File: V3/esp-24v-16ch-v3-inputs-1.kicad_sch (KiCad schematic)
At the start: 100 parts, among them U10 OR-3H4-4, U11 OR-3H4-4, U8 OR-3H4-4, U9 OR-3H4-4

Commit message: working on v3
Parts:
- C23, C24, C25, C26, C27, C28, C29, C30, C31, C32, C33, C34, C35, C36, C37, C38: value 33nF/50V/0805 -> 33nF/50V
- D11, D12, D13, D14, D19, D20, D21, D22, D27, D28, D29, D30, D35, D36, D37, D38: footprint Tales:D_MiniMELF -> Tales:D_SOD-123; Case Mini-MELF -> SOD-123; LCSC Part # C8067 -> C19077407; Mfr Semtech -> hongjiacheng; Mfr PN ZMM9V1-M -> BZT52C9V1; Vendor PN C8067 -> C19077407
- R33, R34, R35, R36, R45, R46, R47, R48, R57, R58, R59, R60, R69, R70, R71, R72: value 5,6k/0,1W/0603 -> 5,6k/0,1W
- R37, R38, R39, R40, R49, R50, R51, R52, R61, R62, R63, R64, R73, R74, R75, R76: value 1k8/0,125W/0805 -> 1k8/0,125W
- R41, R42, R43, R44, R53, R54, R55, R56, R65, R66, R67, R68, R77, R78, R79, R80: value 2k2/62,5mW/0402 -> 2k2/62,5mW

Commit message: Final touches to fabrication
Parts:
- D10, D15, D16, D17, D18, D23, D24, D25, D26, D31, D32, D33, D34, D7, D8, D9: Case 0603 -> 0603/1608
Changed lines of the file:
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@@
 			)
 		)
-		(property "Case" "0603"
+		(property "Case" "0603/1608"
 			(at 33.02 46.99 0)
 			(effects
@@
 			)
 		)
-		(property "Case" "0603"
+		(property "Case" "0603/1608"
 			(at 162.56 120.65 0)
 			(effects
@@
 			)
 		)
-		(property "Case" "0603"
+		(property "Case" "0603/1608"
 			(at 97.79 83.82 0)
 			(effects
@@
 			)
 		)
-		(property "Case" "0603"
+		(property "Case" "0603/1608"
 			(at 33.02 83.82 0)
 			(effects
@@
 			)
 		)
-		(property "Case" "0603"
+		(property "Case" "0603/1608"
 			(at 97.79 46.99 0)
 			(effects
@@
 			)
 		)
-		(property "Case" "0603"
+		(property "Case" "0603/1608"
 			(at 227.33 120.65 0)
 			(effects
@@
 			)
 		)
-		(property "Case" "0603"
+		(property "Case" "0603/1608"
 			(at 227.33 46.99 0)
 			(effects
@@
 			)
 		)
-		(property "Case" "0603"
+		(property "Case" "0603/1608"
 			(at 97.79 120.65 0)
 			(effects
@@
 			)
 		)
-		(property "Case" "0603"
+		(property "Case" "0603/1608"
 			(at 33.02 157.48 0)
 			(effects
@@
 			)
 		)
-		(property "Case" "0603"
+		(property "Case" "0603/1608"
 			(at 227.33 83.82 0)
 			(effects
@@
 			)
 		)
-		(property "Case" "0603"
+		(property "Case" "0603/1608"
 			(at 162.56 83.82 0)
 			(effects
@@
 			)
 		)
-		(property "Case" "0603"
+		(property "Case" "0603/1608"
 			(at 33.02 120.65 0)
 			(effects
@@
 			)
 		)
-		(property "Case" "0603"
+		(property "Case" "0603/1608"
 			(at 162.56 46.99 0)
 			(effects
@@
 			)
 		)
-		(property "Case" "0603"
+		(property "Case" "0603/1608"
 			(at 227.33 157.48 0)
 			(effects
@@
 			)
 		)
-		(property "Case" "0603"
+		(property "Case" "0603/1608"
 			(at 97.79 157.48 0)
 			(effects
@@
 			)
 		)
-		(property "Case" "0603"
+		(property "Case" "0603/1608"
 			(at 162.56 157.48 0)
 			(effects

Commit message: Added temperature sensor
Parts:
- R33, R34, R35, R36, R45, R46, R47, R48, R57, R58, R59, R60, R69, R70, R71, R72: value 5,6k/0,1W -> 5,6k/100mW
- R37, R38, R39, R40, R49, R50, R51, R52, R61, R62, R63, R64, R73, R74, R75, R76: value 1k8/0,125W -> 1k8/125mW
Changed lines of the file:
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@@
 			)
 		)
-		(property "Value" "5,6k/0,1W"
+		(property "Value" "5,6k/100mW"
 			(at 224.79 76.2 0)
 			(effects
@@
 			)
 		)
-		(property "Value" "1k8/0,125W"
+		(property "Value" "1k8/125mW"
 			(at 171.45 27.94 90)
 			(effects
@@
 			)
 		)
-		(property "Value" "5,6k/0,1W"
+		(property "Value" "5,6k/100mW"
 			(at 95.25 113.03 0)
 			(effects
@@
 			)
 		)
-		(property "Value" "1k8/0,125W"
+		(property "Value" "1k8/125mW"
 			(at 236.22 138.43 90)
 			(effects
@@
 			)
 		)
-		(property "Value" "1k8/0,125W"
+		(property "Value" "1k8/125mW"
 			(at 106.68 101.6 90)
 			(effects
@@
 			)
 		)
-		(property "Value" "1k8/0,125W"
+		(property "Value" "1k8/125mW"
 			(at 106.68 27.94 90)
 			(effects
@@
 			)
 		)
-		(property "Value" "5,6k/0,1W"
+		(property "Value" "5,6k/100mW"
 			(at 224.79 113.03 0)
 			(effects
@@
 			)
 		)
-		(property "Value" "5,6k/0,1W"
+		(property "Value" "5,6k/100mW"
 			(at 30.48 39.37 0)
 			(effects
@@
 			)
 		)
-		(property "Value" "1k8/0,125W"
+		(property "Value" "1k8/125mW"
 			(at 41.91 101.6 90)
 			(effects
@@
 			)
 		)
-		(property "Value" "5,6k/0,1W"
+		(property "Value" "5,6k/100mW"
 			(at 224.79 39.37 0)
 			(effects
@@
 			)
 		)
-		(property "Value" "5,6k/0,1W"
+		(property "Value" "5,6k/100mW"
 			(at 30.48 113.03 0)
 			(effects
@@
 			)
 		)
-		(property "Value" "5,6k/0,1W"
+		(property "Value" "5,6k/100mW"
 			(at 95.25 39.37 0)
 			(effects
@@
 			)
 		)
-		(property "Value" "5,6k/0,1W"
+		(property "Value" "5,6k/100mW"
 			(at 95.25 149.86 0)
 			(effects
@@
 			)
 		)
-		(property "Value" "5,6k/0,1W"
+		(property "Value" "5,6k/100mW"
 			(at 160.02 149.86 0)
 			(effects
@@
 			)
 		)
-		(property "Value" "1k8/0,125W"
+		(property "Value" "1k8/125mW"
 			(at 106.68 64.77 90)
 			(effects
@@
 			)
 		)
-		(property "Value" "1k8/0,125W"
+		(property "Value" "1k8/125mW"
 			(at 171.45 64.77 90)
 			(effects
@@
 			)
 		)
-		(property "Value" "1k8/0,125W"
+		(property "Value" "1k8/125mW"
 			(at 106.68 138.43 90)
 			(effects
@@
 			)
 		)
-		(property "Value" "5,6k/0,1W"
+		(property "Value" "5,6k/100mW"
 			(at 95.25 76.2 0)
 			(effects
@@
 			)
 		)
-		(property "Value" "5,6k/0,1W"
+		(property "Value" "5,6k/100mW"
 			(at 160.02 76.2 0)
 			(effects
@@
 			)
 		)
-		(property "Value" "1k8/0,125W"
+		(property "Value" "1k8/125mW"
 			(at 236.22 64.77 90)
 			(effects
@@
 			)
 		)
-		(property "Value" "1k8/0,125W"
+		(property "Value" "1k8/125mW"
 			(at 171.45 101.6 90)
 			(effects
@@
 			)
 		)
-		(property "Value" "1k8/0,125W"
+		(property "Value" "1k8/125mW"
 			(at 41.91 64.77 90)
 			(effects
@@
 			)
 		)
-		(property "Value" "5,6k/0,1W"
+		(property "Value" "5,6k/100mW"
 			(at 224.79 149.86 0)
 			(effects
@@
 			)
 		)
-		(property "Value" "5,6k/0,1W"
+		(property "Value" "5,6k/100mW"
 			(at 30.48 76.2 0)
 			(effects
@@
 			)
 		)
-		(property "Value" "1k8/0,125W"
+		(property "Value" "1k8/125mW"
 			(at 236.22 27.94 90)
 			(effects
@@
 			)
 		)
-		(property "Value" "5,6k/0,1W"
+		(property "Value" "5,6k/100mW"
 			(at 160.02 39.37 0)
 			(effects
@@
 			)
 		)
-		(property "Value" "5,6k/0,1W"
+		(property "Value" "5,6k/100mW"
 			(at 160.02 113.03 0)
 			(effects
@@
 			)
 		)
-		(property "Value" "1k8/0,125W"
+		(property "Value" "1k8/125mW"
 			(at 236.22 101.6 90)
 			(effects
@@
 			)
 		)
-		(property "Value" "1k8/0,125W"
+		(property "Value" "1k8/125mW"
 			(at 171.45 138.43 90)
 			(effects
@@
 			)
 		)
-		(property "Value" "5,6k/0,1W"
+		(property "Value" "5,6k/100mW"
 			(at 30.48 149.86 0)
 			(effects
@@
 			)
 		)
-		(property "Value" "1k8/0,125W"
+		(property "Value" "1k8/125mW"
 			(at 41.91 138.43 90)
 			(effects
@@
 			)
 		)
-		(property "Value" "1k8/0,125W"
+		(property "Value" "1k8/125mW"
 			(at 41.91 27.94 90)
 			(effects

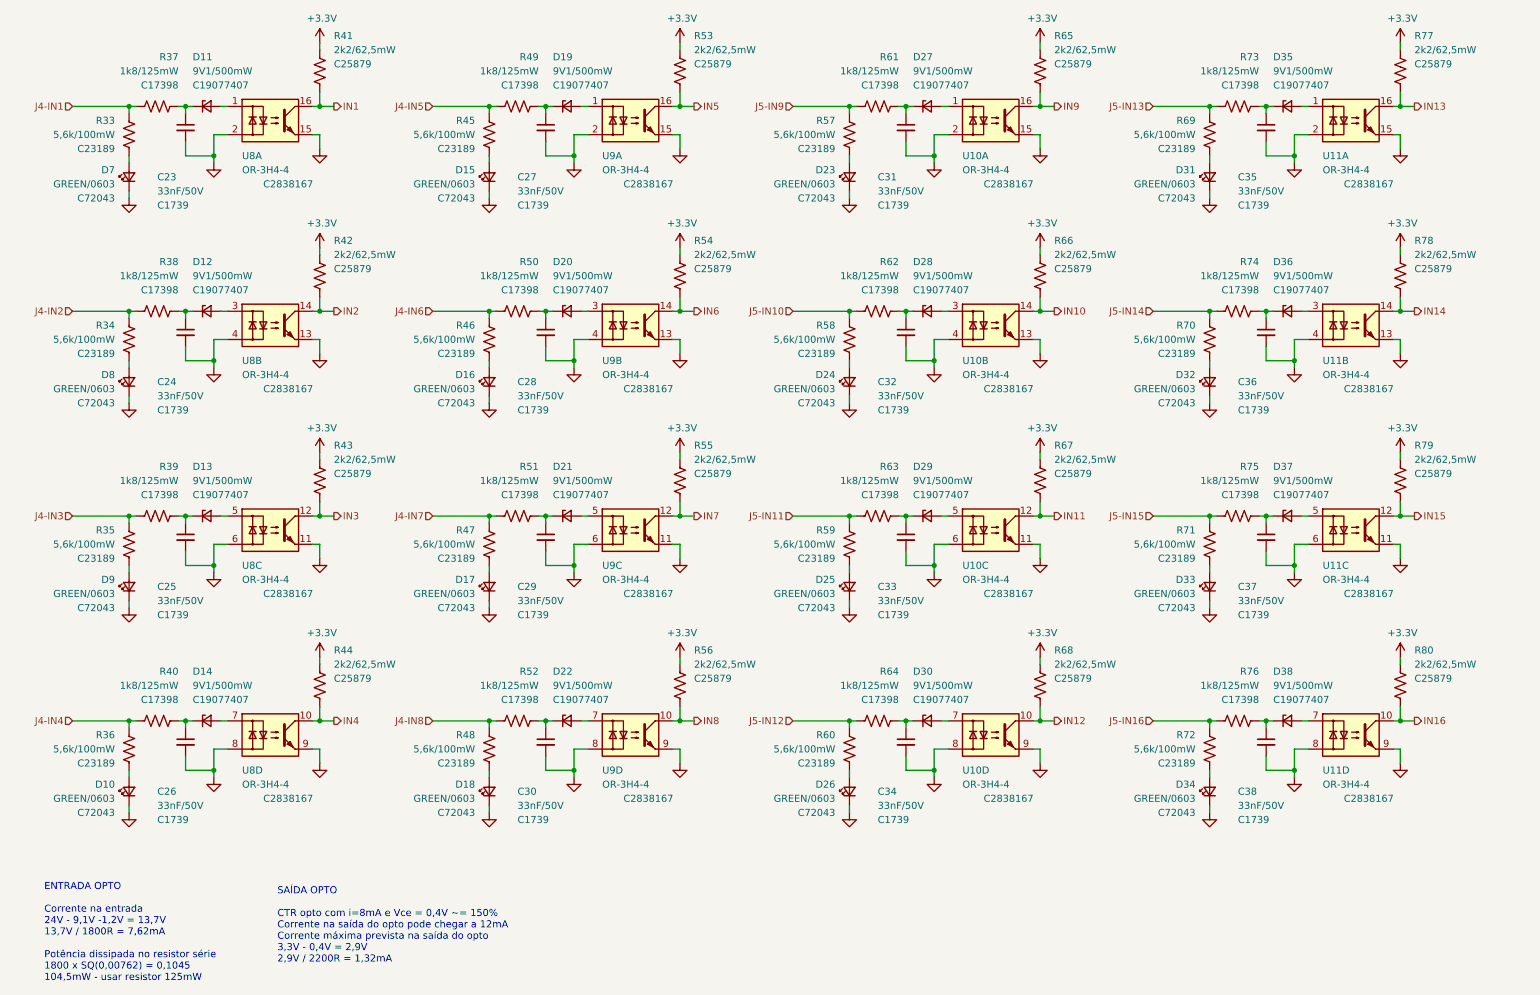
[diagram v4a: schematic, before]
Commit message: Updating component part numbers
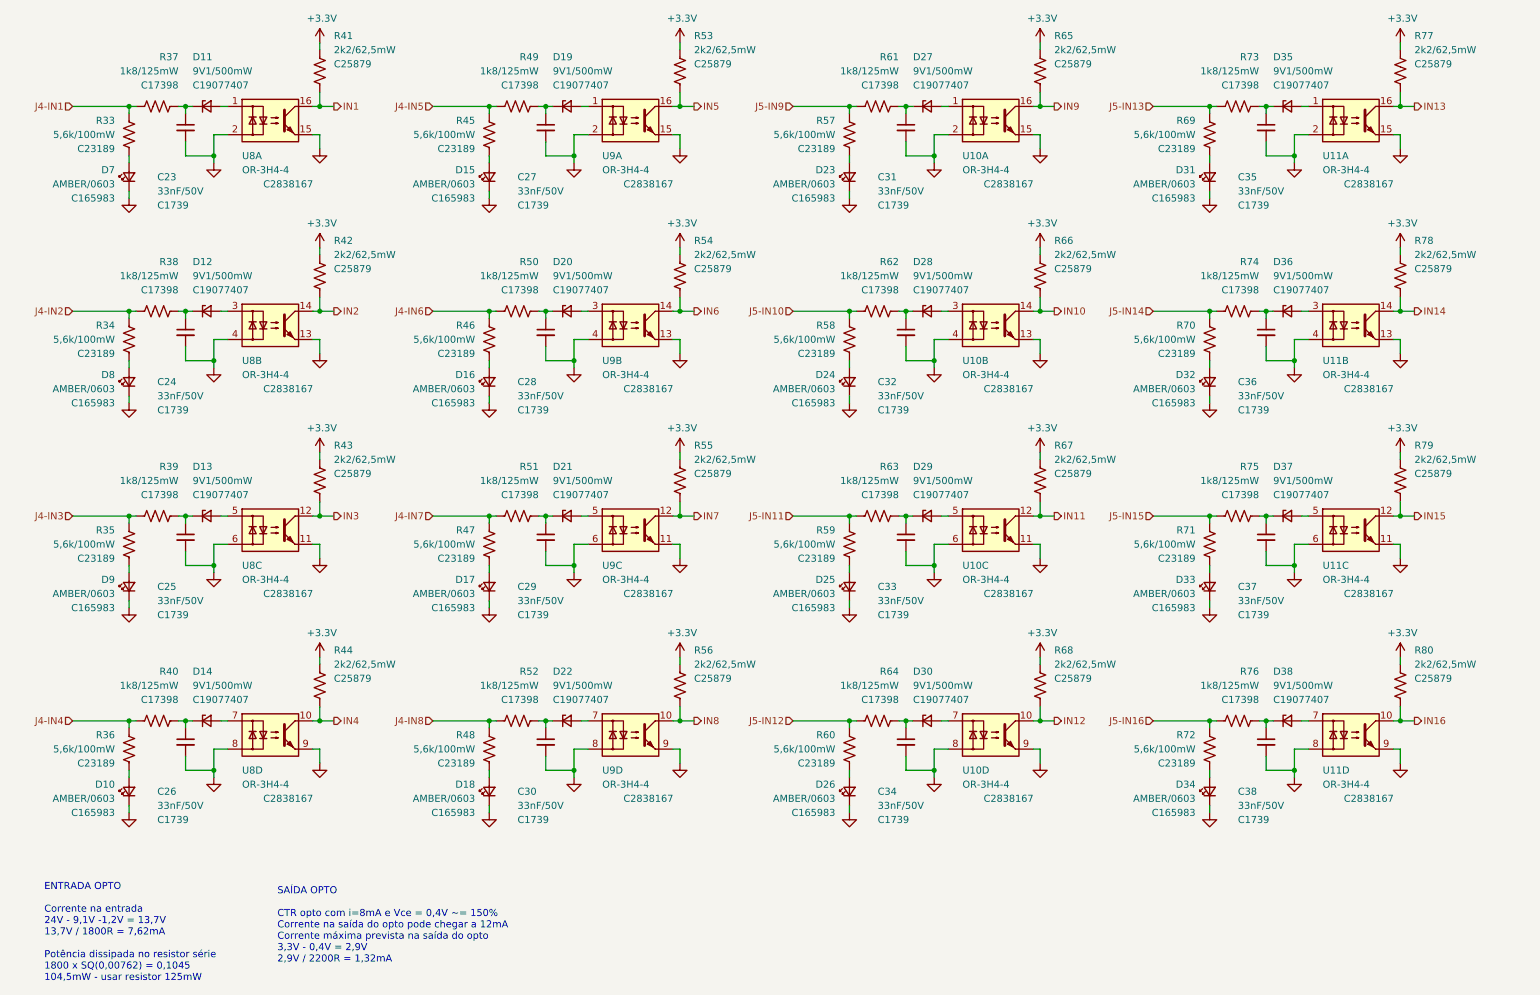
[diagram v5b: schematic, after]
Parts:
- D10, D15, D16, D17, D18, D23, D24, D25, D26, D31, D32, D33, D34, D7, D8, D9: value GREEN/0603 -> AMBER/0603; LCSC Part # C72043 -> C165983; Mfr Everlight -> BrtLed(Bright LED Elec); Mfr PN 19-217/GHC-YR1S2/3T -> BL-HJC36G-AV-TRB; Vendor PN C72043 -> C165983

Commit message: Prefab checks
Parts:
- D10, D15, D16, D17, D18, D23, D24, D25, D26, D31, D32, D33, D34, D7, D8, D9: value AMBER/0603 -> EMERALD/0603; LCSC Part # C165983 -> C2984266; Mfr BrtLed(Bright LED Elec) -> Everlight Elec; Mfr PN BL-HJC36G-AV-TRB -> 19-213/GHC-XS1T1N/5T; Vendor PN C165983 -> C2984266
